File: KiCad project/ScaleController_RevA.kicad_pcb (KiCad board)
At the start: 4 copper layers, 89.9 x 52.8 mm, 57 parts, among them J1 USB_C_Receptacle, J3 MTMM-103-03-T-S-150, J5 MTMM-103-03-T-S-150, J6 Conn_01x05, J7 MTMM-103-03-T-S-150, J8 MTMM-103-03-T-S-150, J9 Conn_01x04_Socket, Q2 BC817, Q3 BC817, SW1 1101NE, SW2 1101NE, U2 LM1117MPX-3.3_NOPB, U3 ESP32-C3-WROOM-02-H4, U4 CP2102N-A02-GQFN20, U5 USBLC6-2SC6, U6 HX711

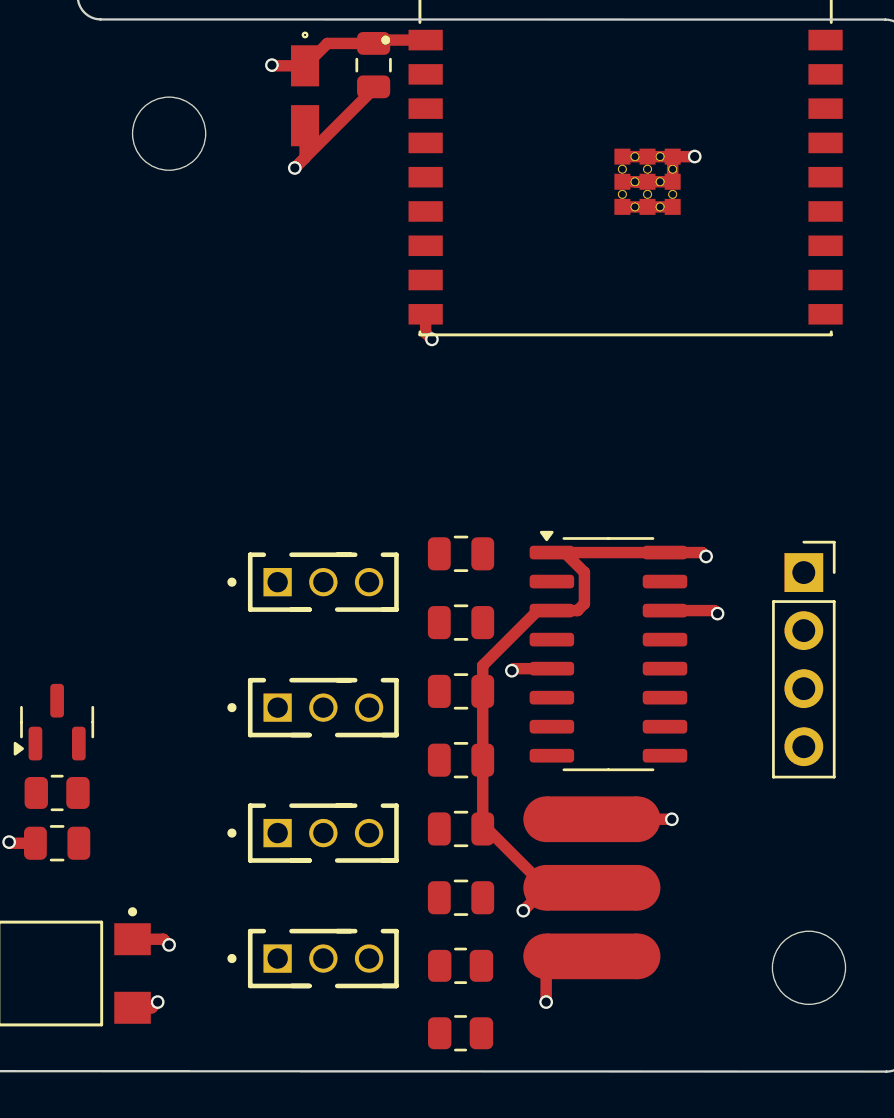
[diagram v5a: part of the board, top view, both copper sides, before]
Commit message: Route HX711 analog section; re-place filter parts and net ties
Placement: J5/J7 swapped so S+ connectors (J3, J7) and S- connectors
(J5, J8) are adjacent; cap/resistor column re-ordered pin-by-pin
(C16, C15, C14 supply caps at top; C17 by VBG; R16/C13 by INA-;
R15/C12 by INA+); NT2 moved beside the connectors with its own 3.3V
via; NT3 moved to the bottom edge by the connectors with its own GND via.

Routing (F.Cu unless noted): E+ chain through connector pin 1; E- chain
on B.Cu through pin 3; S+/S- to the 100R filters; INA+/INA- from the
filter nodes with shunt caps to AGND; VBG bypass; AGND network (left
column, U6 pins 4/9/10/15) meeting GND only at NT1; DOUT on F.Cu and
PD_SCK on B.Cu to the ESP32-C3. Removed the stub/via to NT2's and NT3's
old positions and the superseded 3.3V column chain.

Verified on a fill-stripped copy: 0 clearance violations. Zone fills in
this commit are stale; refill in the GUI. 37 digital connections remain.

Co-Authored-By: Claude Fable 5.1 <noreply@anthropic.com>
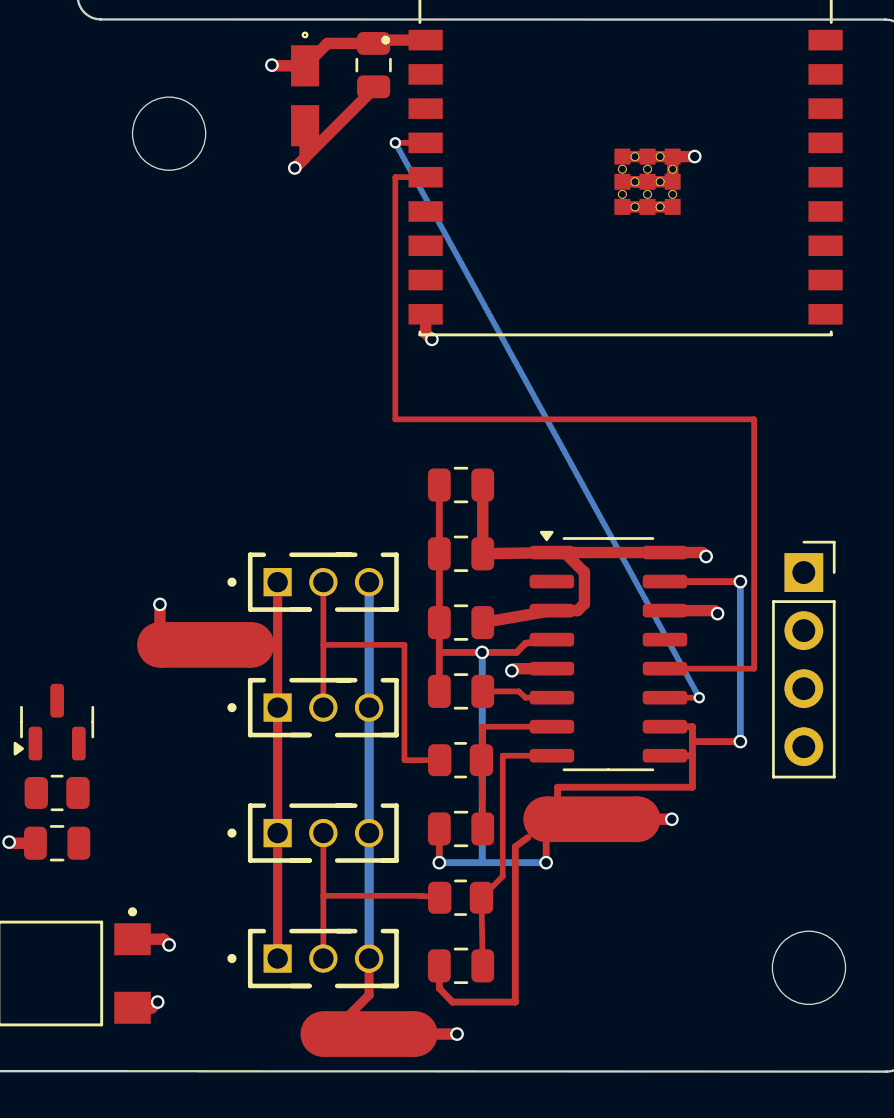
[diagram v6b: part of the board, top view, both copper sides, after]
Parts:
- moved NT2 20.0 mm to (170.6, 106.4)
- moved C12 18.0 mm to (181.8, 120.4)
- moved C16 15.0 mm to (181.8, 99.4)
- moved R16 11.9 mm to (181.8, 111.4), turned to 180 degrees
- moved J3 11.0 mm to (173.8, 114.6)
- moved J8 11.0 mm to (173.8, 109.1)
- moved NT3 10.3 mm to (177.8, 123.4), turned to 180 degrees
- moved C13 9.03 mm to (181.8, 114.4), turned to 180 degrees
- moved C15 9.03 mm to (181.8, 102.4)
- moved C17 9.03 mm to (181.8, 108.4), turned to 180 degrees
- moved J5 5.49 mm to (173.8, 103.6)
- moved J7 5.49 mm to (173.8, 120.1)
- moved C14 3.01 mm to (181.8, 105.4)
- moved R15 2.98 mm to (181.8, 117.4), turned to 180 degrees
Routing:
- net /HX711_LoadCell_Summing/AGND: track 0.00 -> 66.8 mm, vias 0 -> 5
- net /ESP32-C3-02/DOUT: track 0.00 -> 42.4 mm
- net /ESP32-C3-02/PD_SCK: track 0.00 -> 30.5 mm, vias 0 -> 2
- net /HX711_LoadCell_Summing/E-: track 0.00 -> 20.7 mm
- net /HX711_LoadCell_Summing/E+: track 0.00 -> 17.6 mm
- net /HX711_LoadCell_Summing/S_MINUS_GRP: track 0.00 -> 15.6 mm
- net /HX711_LoadCell_Summing/A+: track 0.00 -> 11.7 mm
- net /HX711_LoadCell_Summing/S_PLUS_GRP: track 0.00 -> 10.6 mm
- net /HX711_LoadCell_Summing/A-: track 0.00 -> 7.56 mm
- net 3.3V: track 74.5 -> 69.6 mm
- net Net-(U6-VBG): track 0.00 -> 3.13 mm
